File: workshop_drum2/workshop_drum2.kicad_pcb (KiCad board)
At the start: 2 copper layers, 62.2 x 45 mm, 40 parts, among them J1 9v_Battery_Clip, J2 Trigger_Input, J3 Output, U1 LM358, U2 7414, U3 78L05

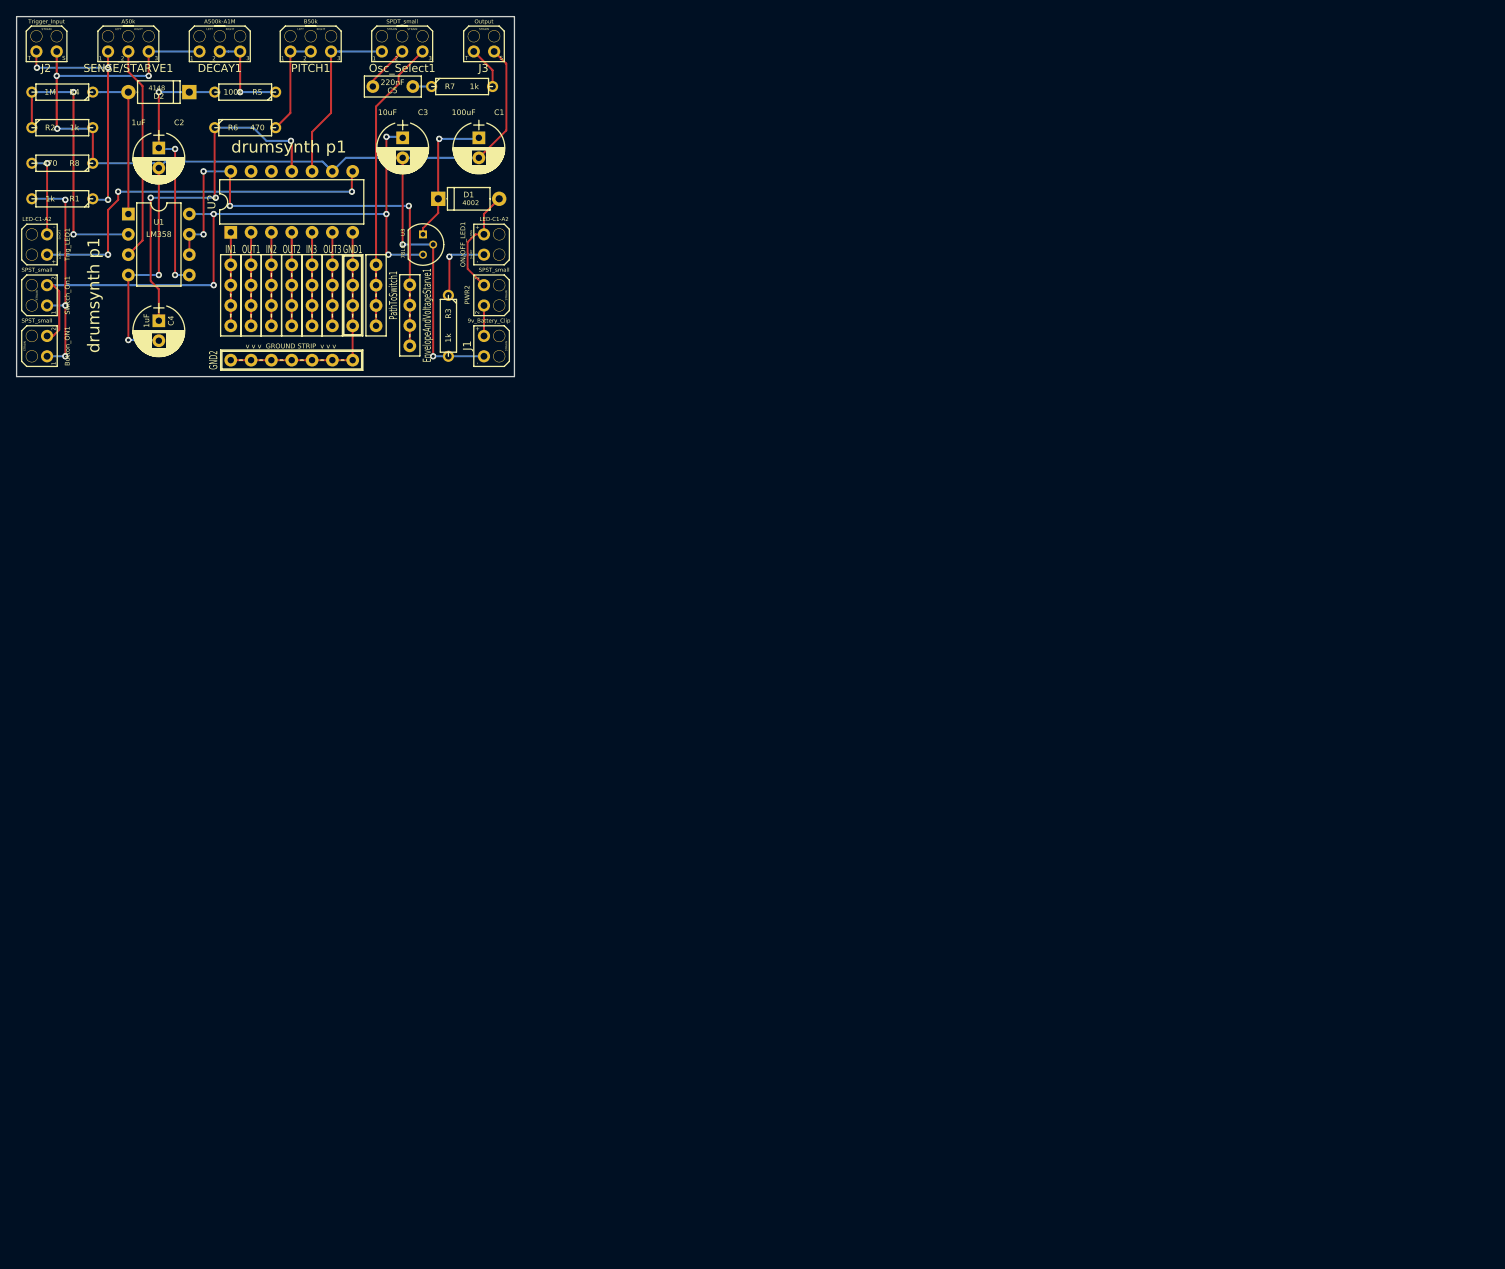
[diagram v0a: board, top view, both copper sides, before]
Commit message: P1.1 - Updated footprints prior to deleting PCB
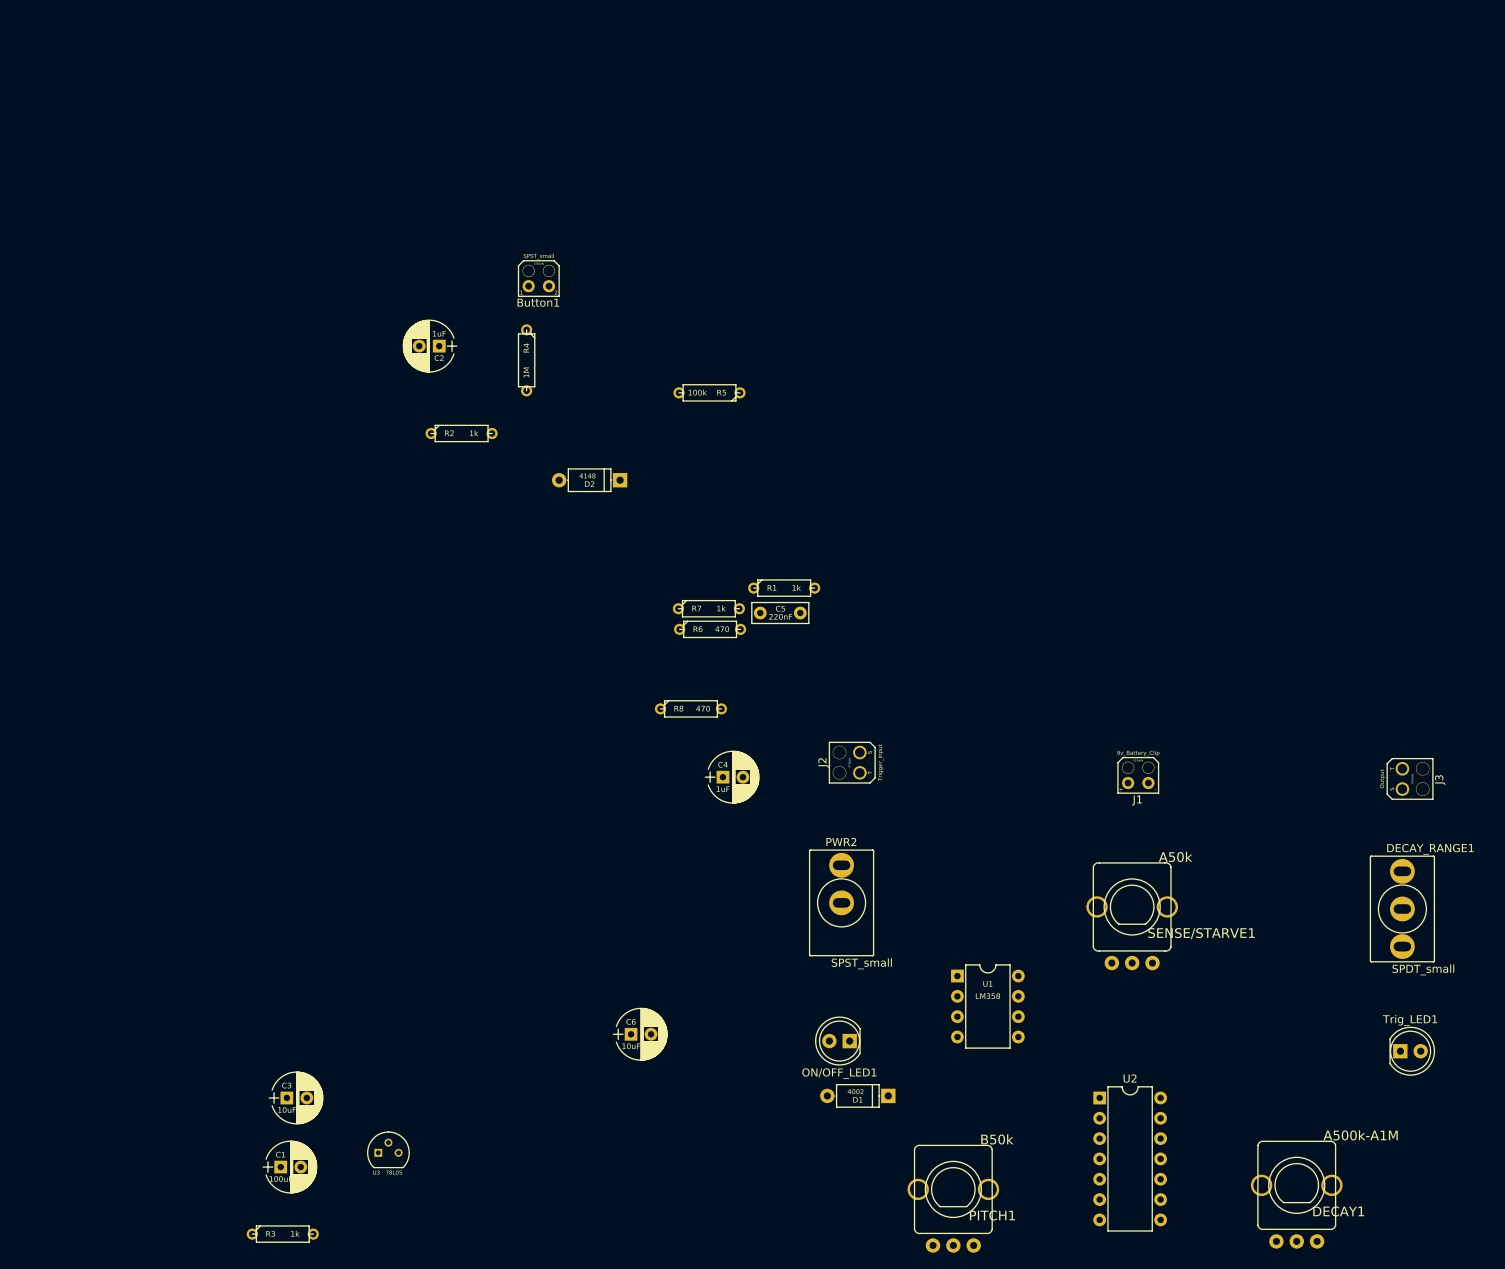
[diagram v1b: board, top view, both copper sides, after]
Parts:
- removed Button_ON1, Switch_On1: SPST_small, zfoot:SPST_Wired
- removed EnvelopeAndVoltageStarve1: PWRStrip, zfoot:BreadBoardStrip_4
- removed GND1: GNDStrip, zfoot:BreadBoardStripBold_4
- removed GND2: GNDStrip, zfoot:BreadBoardStripBold_7
- removed IN1, IN2, IN3, OUT1, OUT2, OUT3, PathToSwitch1: BreadBoardStrip, zfoot:BreadBoardStrip_4
- removed Osc_Select1: SPDT_small, zfoot:SPDT_Wired
- added Button1: SPST_small, zfoot:SPST_Wired, F.Cu at (65.3, -11.3)
- added C6: 10uF, 4ms-footprints:Cap_Electrolytic_TH, F.Cu at (76.8, 82.2)
- added DECAY_RANGE1: SPDT_small, zfoot:Switch_Toggle_SPDT_Mini_SolderLug, F.Cu at (173.2, 66.5)
- DECAY1, PITCH1, SENSE/STARVE1: footprint zfoot:Pot_Wired -> zfoot:POT-9MM-ALPHA
- J2, J3: footprint zfoot:Jack_Instrument -> zfoot:Jack_Instrument_Bigger
- ON/OFF_LED1, Trig_LED1: footprint zfoot:LED_wired -> zfoot:LED_D5.0mm
- PWR2: footprint zfoot:SPST_Wired -> zfoot:Switch_Toggle_SPST_Mini_SolderLug_2legs
- moved Trig_LED1 196.9 mm to (173.0, 84.3), turned to 0 degrees
- moved DECAY1 195.5 mm to (160.0, 101.1), turned to 180 degrees
- moved SENSE/STARVE1 164.9 mm to (139.4, 66.3), turned to 180 degrees
- moved PITCH1 163.4 mm to (117.1, 101.6), turned to 180 degrees
- moved U2 153.3 mm to (135.4, 90.2), turned to 0 degrees
- moved J3 146.5 mm to (173.2, 50.3), turned to 270 degrees
- moved U1 140.8 mm to (117.6, 74.9)
- moved J2 135.1 mm to (105.4, 48.3), turned to 90 degrees
- moved C1 131.0 mm to (33.0, 98.8), turned to 0 degrees
- moved D1 125.5 mm to (109.0, 89.9), turned to 180 degrees
- moved C3 120.9 mm to (33.8, 90.2), turned to 0 degrees
- moved R3 115.4 mm to (33.3, 107.2), turned to 0 degrees
- moved U3 114.9 mm to (45.2, 97.0), turned to 0 degrees
- moved ON/OFF_LED1 109.6 mm to (104.1, 83.1), turned to 180 degrees
- moved R8 104.1 mm to (84.3, 41.5), turned to 0 degrees
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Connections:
- D2 pad 1: Net-(C2-Pad1) -> Net-(D2-Pad1)
- PITCH1 pad 3: Net-(Osc_Select1-Pad1) -> Net-(C5-Pad2)
- R5 pad 2: Net-(C2-Pad1) -> Net-(D2-Pad1)
- U1 pad 5: Net-(C2-Pad1) -> Net-(D2-Pad1)
- U2 pad 10: Net-(Osc_Select1-Pad1) -> Net-(C5-Pad2)
- U2 pad 7: Net-(GND1-Pad1) -> GND
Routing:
- net GND: track 169.0 -> 0.00 mm, vias 7 -> 0
- net +5V: track 84.1 -> 0.00 mm, vias 5 -> 0
- net Net-(U1-Pad6): track 60.0 -> 0.00 mm, vias 4 -> 0
- net Net-(Trig_LED1-Pad2): track 47.8 -> 0.00 mm, vias 3 -> 0
- net Net-(C4-Pad1): track 46.8 -> 0.00 mm, vias 3 -> 0
- net Net-(Osc_Select1-Pad3): track 36.7 -> 0.00 mm
- net Net-(R2-Pad1): track 34.3 -> 0.00 mm, vias 2 -> 0
- net Net-(C2-Pad1): track 33.6 -> 0.00 mm, vias 3 -> 0
- net Net-(J2-Pad1): track 31.4 -> 0.00 mm, vias 3 -> 0
- net Net-(GND1-Pad1): track 31.2 -> 0.00 mm
- net Net-(Button1-Pad1): track 28.4 -> 0.00 mm, vias 3 -> 0
- net Net-(SENSE/STARVE1-Pad2): track 26.9 -> 0.00 mm
- net Net-(Osc_Select1-Pad1): track 22.3 -> 0.00 mm
- net Net-(D2-Pad2): track 19.7 -> 0.00 mm
- net Net-(C1-Pad1): track 17.8 -> 0.00 mm, vias 1 -> 0
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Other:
- board outline removed
- rule pad_to_mask_clearance: 0.2 -> 0
- board text removed: "drumsynth p1"
- board text removed: "v v v GROUND STRIP v v v"
